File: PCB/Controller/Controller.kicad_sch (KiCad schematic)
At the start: 2 parts

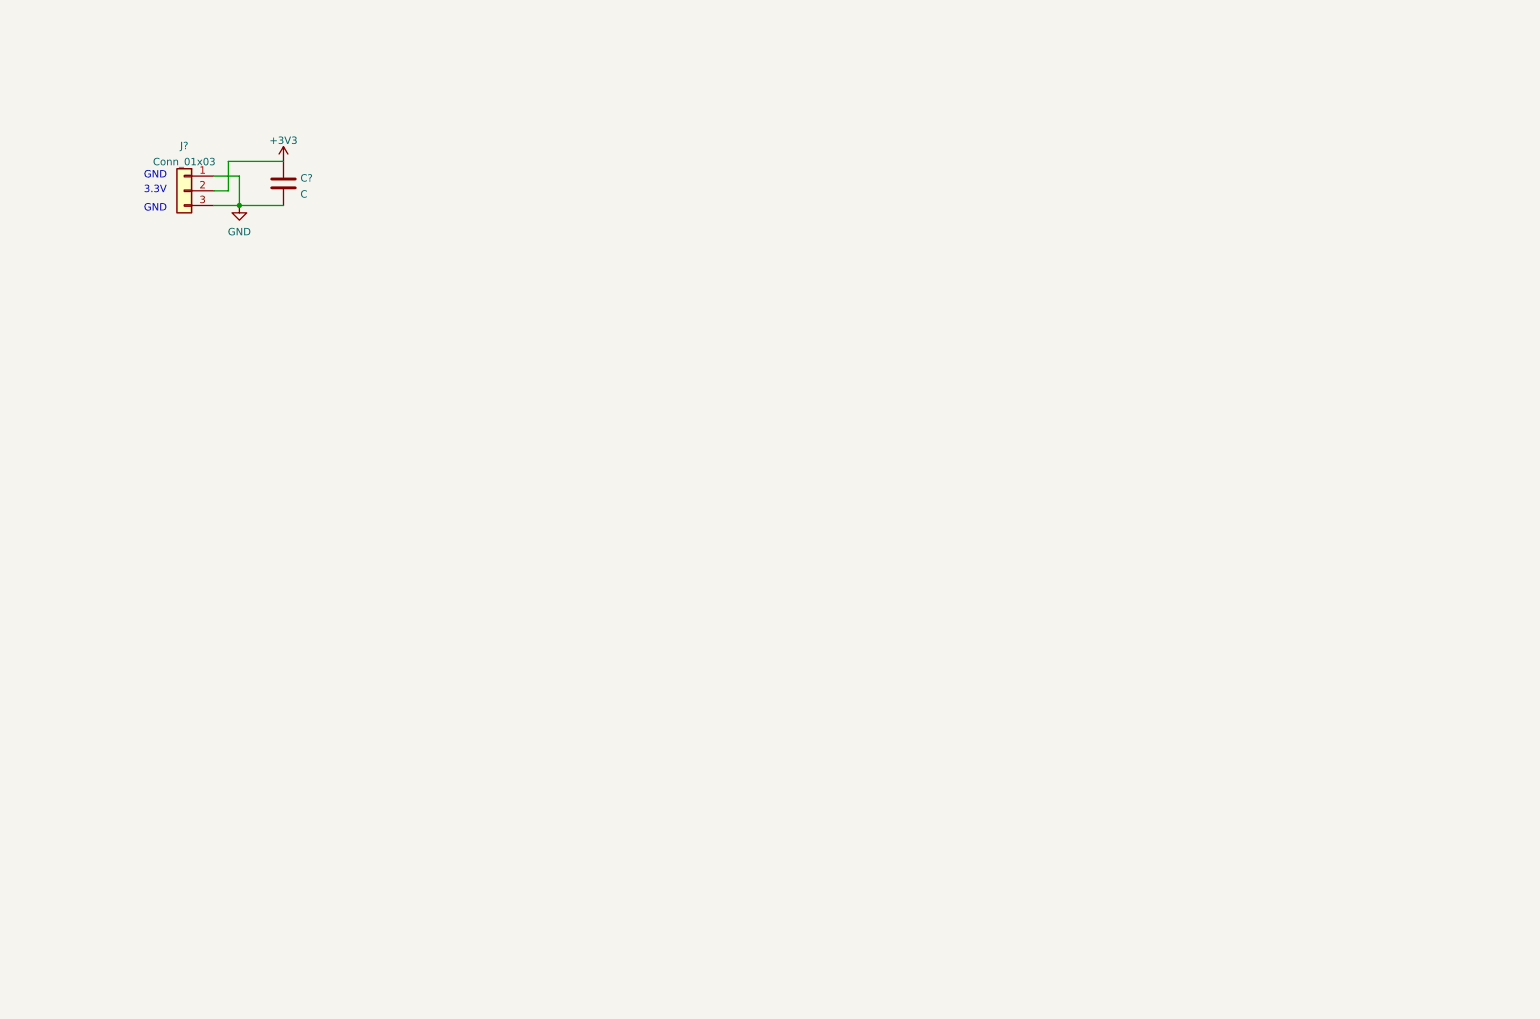
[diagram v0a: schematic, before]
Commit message: sample bdf font script.
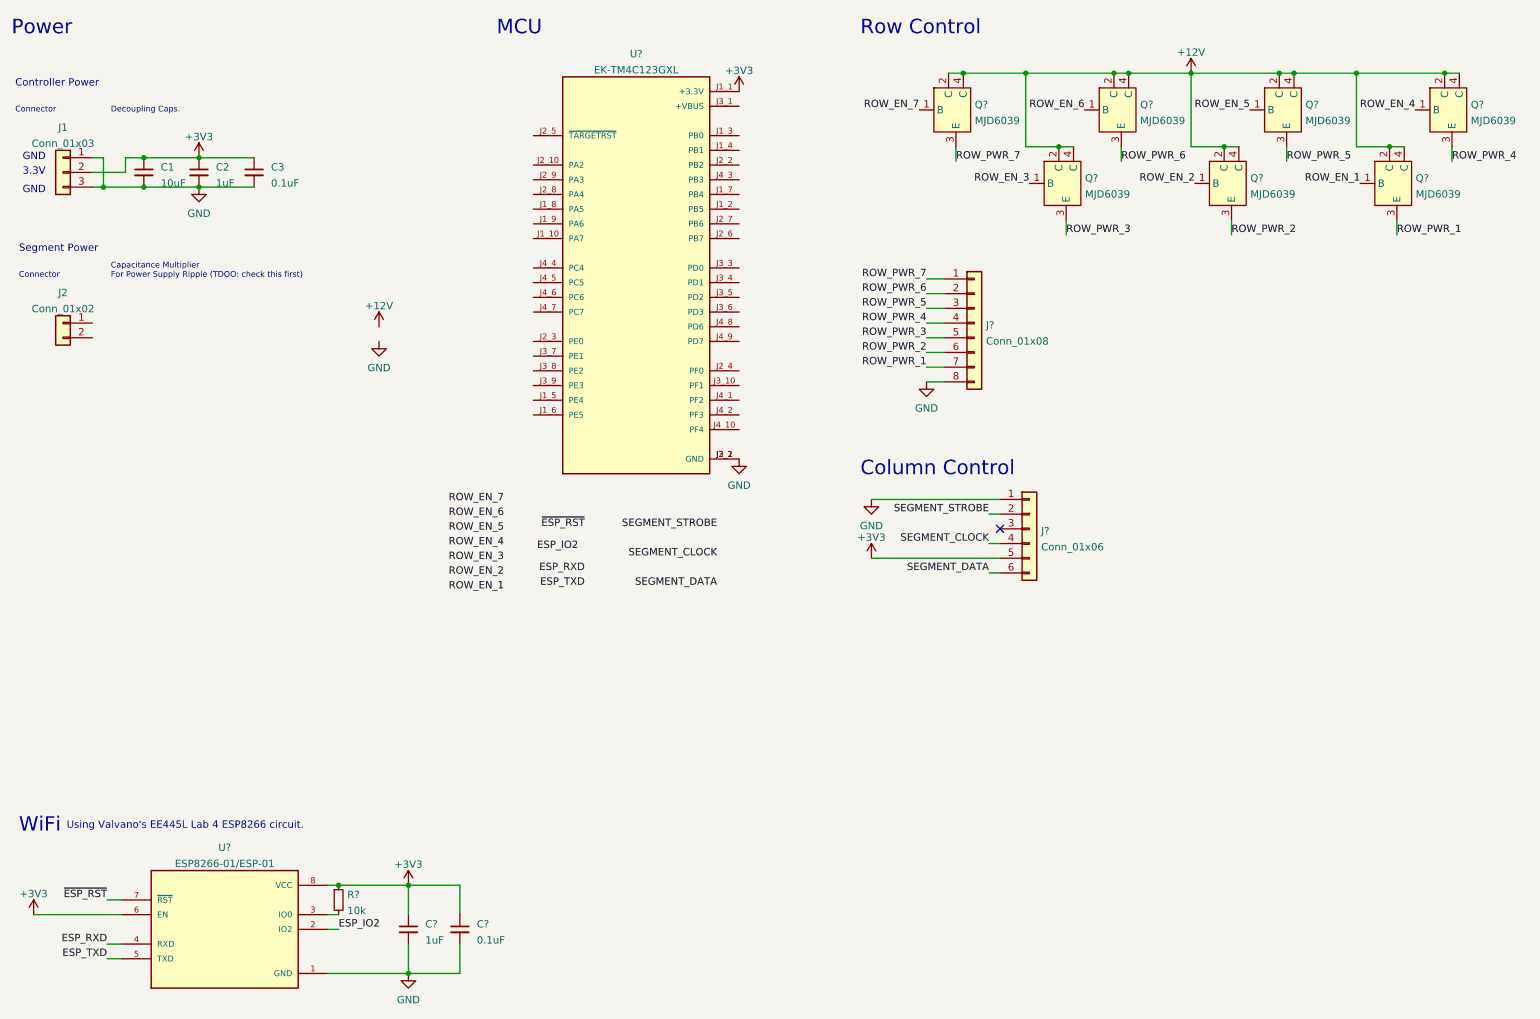
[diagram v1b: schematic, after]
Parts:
- added C1: 10uF, symbol Device:C_Small
- added C3, C?: 0.1uF, symbol Device:C_Small
- added C?: 1uF, symbol Device:C_Small
- added J2: Conn_01x02, symbol Connector_Generic:Conn_01x02
- added J?: Conn_01x06, symbol Connector_Generic:Conn_01x06
- added J?: Conn_01x08, symbol Connector_Generic:Conn_01x08
- added Q? (x7): MJD6039, symbol MJD6039:MJD6039
- added R?: 10k, symbol Device:R_Small
- added U?: ESP8266-01/ESP-01, Footprints:XCVR_ESP8266-01_ESP-01, symbol ESP8266-01_ESP-01:ESP8266-01{brace}slash}ESP-01
- added U?: EK-TM4C123GXL, Footprints:MODULE_EK-TM4C123GXL, symbol EK-TM4C123GXL:EK-TM4C123GXL
- C2: renamed from C?; value C -> 1uF; symbol Device:C -> Device:C_Small
- gave numbers to parts that had none: 1
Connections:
- net +3V3: now also C1.1, C3.1, C?.1, C?.1, J?.5 (Pin_5), R?.1, U?.6 (EN), U?.8 (VCC), U?.J1_1 (+3.3V)
- net GND: now also C1.2, C3.2, C?.2, C?.2, J?.1 (Pin_1), J?.8 (Pin_8), U?.1 (GND), U?.J2_1 (GND), U?.J3_2 (GND)
- new net: R?.2, U?.3 (IO0)
- new net +12V: Q?.2 (C), Q?.2 (C), Q?.2 (C), Q?.2 (C), Q?.2 (C), Q?.2 (C), Q?.2 (C), Q?.4 (C), Q?.4 (C), Q?.4 (C), Q?.4 (C), Q?.4 (C), Q?.4 (C), Q?.4 (C)
- new net ESP_IO2: U?.2 (IO2)
- new net ESP_RXD: U?.4 (RXD)
- new net ESP_TXD: U?.5 (TXD)
- new net ROW_EN_1: Q?.1 (B)
- new net ROW_EN_2: Q?.1 (B)
- new net ROW_EN_3: Q?.1 (B)
- new net ROW_EN_4: Q?.1 (B)
- new net ROW_EN_5: Q?.1 (B)
- new net ROW_EN_6: Q?.1 (B)
- new net ROW_EN_7: Q?.1 (B)
- new net ROW_PWR_1: J?.7 (Pin_7), Q?.3 (E)
- new net ROW_PWR_2: J?.6 (Pin_6), Q?.3 (E)
- new net ROW_PWR_3: J?.5 (Pin_5), Q?.3 (E)
- new net ROW_PWR_4: J?.4 (Pin_4), Q?.3 (E)
- new net ROW_PWR_5: J?.3 (Pin_3), Q?.3 (E)
- new net ROW_PWR_6: J?.2 (Pin_2), Q?.3 (E)
- new net ROW_PWR_7: J?.1 (Pin_1), Q?.3 (E)
- new net SEGMENT_CLOCK: J?.4 (Pin_4)
- new net SEGMENT_DATA: J?.6 (Pin_6)
- new net SEGMENT_STROBE: J?.2 (Pin_2)
- new net ~{ESP_RST}: U?.7 (~{RST})
- no-connect marks 0 -> 1
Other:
- note added: "Capacitance Multiplier For Power Supply Ripple (TDOO: check this first)"
- note added: "Column Control"
- note added: "Connector"
- note added: "Controller Power"
- note added: "Decoupling Caps."
- note added: "MCU"
- note added: "Power"
- note added: "Row Control"
- note added: "Segment Power"
- note added: "Using Valvano's EE445L Lab 4 ESP8266 circuit."
- note added: "WiFi"
- company: (none) -> IEEE RAS UT
- title: (none) -> Marquee Signboard Controller
- moved on the sheet: C2, J1

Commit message: finished v1.0.0 of marquee controller.
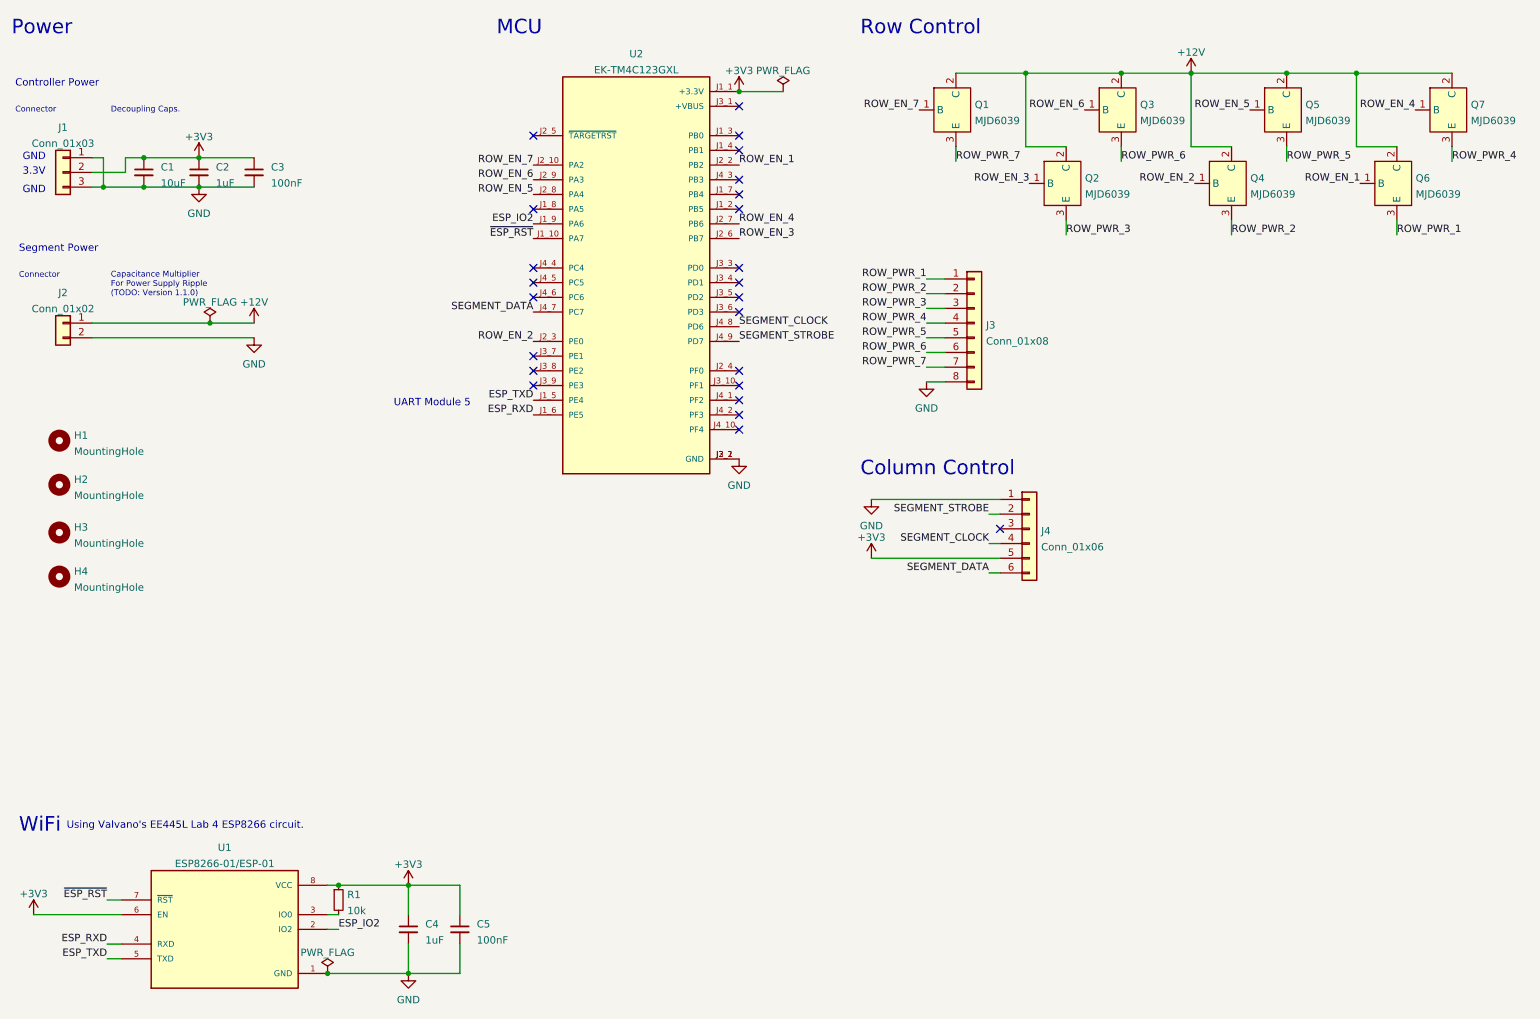
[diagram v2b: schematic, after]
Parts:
- added H1, H2, H3, H4: MountingHole, MountingHole:MountingHole_2.2mm_M2, symbol Mechanical:MountingHole
- C1: footprint (none) -> Capacitor_SMD:C_0805_2012Metric; Distributor (none) -> JLCPCB; JLCPCB BOM (none) -> 1; LCSC Part (none) -> C15850; Manufacturer (none) -> Samsung Electro-Mechanics; Part Number (none) -> CL21A106KAYNNNE; Projected Cost (none) -> 0.0148
- C2: footprint (none) -> Capacitor_SMD:C_0805_2012Metric; Distributor (none) -> JLCPCB; JLCPCB BOM (none) -> 1; LCSC Part (none) -> C28323; Manufacturer (none) -> Samsung Electro-Mechanics; Part Number (none) -> CL21B105KBFNNNE; Projected Cost (none) -> 0.0096
- C3: value 0.1uF -> 100nF; footprint (none) -> Capacitor_SMD:C_0805_2012Metric; Distributor (none) -> JLCPCB; JLCPCB BOM (none) -> 1; LCSC Part (none) -> C49678; Manufacturer (none) -> Yageo; Part Number (none) -> CC0805KRX7R9BB104; Projected Cost (none) -> 0.0048
- C4: renamed from C?; footprint (none) -> Capacitor_SMD:C_0805_2012Metric; Distributor (none) -> JLCPCB; JLCPCB BOM (none) -> 1; LCSC Part (none) -> C28323; Manufacturer (none) -> Samsung Electro-Mechanics; Part Number (none) -> CL21B105KBFNNNE; Projected Cost (none) -> 0.0096
- C5: renamed from C?; value 0.1uF -> 100nF; footprint (none) -> Capacitor_SMD:C_0805_2012Metric; Distributor (none) -> JLCPCB; JLCPCB BOM (none) -> 1; LCSC Part (none) -> C49678; Manufacturer (none) -> Yageo; Part Number (none) -> CC0805KRX7R9BB104; Projected Cost (none) -> 0.0048
- J1: footprint (none) -> Connector_PinHeader_2.54mm:PinHeader_1x03_P2.54mm_Vertical
- J2: footprint (none) -> Connector_Wire:SolderWire-2.5sqmm_1x02_P7.2mm_D2.4mm_OD3.6mm
- J3: renamed from J?; footprint (none) -> Footprints:SolderWire-2sqmm_1x08_P7.8mm_D2mm_OD3.9mm
- J4: renamed from J?; footprint (none) -> Connector_Wire:SolderWire-2.5sqmm_1x06_P8.8mm_D2.4mm_OD4.4mm
- Q1, Q2, Q3, Q4, Q5, Q6, Q7: renamed from Q?; footprint (none) -> Package_TO_SOT_SMD:TO-252-3_TabPin2; Distributor (none) -> Mouser; JLCPCB BOM (none) -> 0; Manufacturer (none) -> ONSEMI; Part Number (none) -> MJD6039T4G; Projected Cost (none) -> 0.9; Purchase Page (none) -> https://www.mouser.com/ProductDetail/onsemi/MJD6039T4G?qs=H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
- R1: renamed from R?; footprint (none) -> Resistor_SMD:R_0805_2012Metric; Distributor (none) -> JLCPCB; JLCPCB BOM (none) -> 1; LCSC Part (none) -> C17724; Manufacturer (none) -> Uniroyal Elec; Part Number (none) -> 0805W8F510KT5E; Projected Cost (none) -> 0.0038
- U1: renamed from U?; Distributor (none) -> Mouser; JLCPCB BOM (none) -> 0; MANUFACTURER AI-Thinker -> (none); MAXIMUM_PACKAGE_HEIGHT 11.2 mm -> (none); Manufacturer (none) -> SparkFun; PARTREV V1.2 -> (none); Part Number (none) -> WRL-17146; Projected Cost (none) -> 6.95; Purchase Page (none) -> https://www.mouser.com/ProductDetail/SparkFun/WRL-17146?qs=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; STANDARD Manufacturer recommendations or IPC 7351B -> (none)
- U2: renamed from U?; Alternative Part (none) -> https://www.ti.com/tool/EK-TM4C123GXL; Distributor (none) -> Mouser; JLCPCB BOM (none) -> 0; MANUFACTURER Texas Instruments -> (none); MAXIMUM_PACKAGE_HIEGHT N/A -> (none); Manufacturer (none) -> Texas Instruments; PARTREV April 2013 -> (none); Part Number (none) -> EK-TM4C123GXL; Projected Cost (none) -> 22.60; Purchase Page (none) -> https://www.mouser.com/ProductDetail/Texas-Instruments/EK-T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; STANDARD Manufacturer Recommendations -> (none)
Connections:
- net +12V: now also J2.1 (Pin_1); no longer Q1.4 (C), Q2.4 (C), Q3.4 (C), Q4.4 (C), Q5.4 (C), Q6.4 (C), Q7.4 (C)
- net ESP_IO2: now also U2.J1_9 (PA6)
- net ESP_RXD: now also U2.J1_6 (PE5)
- net ESP_TXD: now also U2.J1_5 (PE4)
- net GND: now also J2.2 (Pin_2)
- net ROW_EN_1: now also U2.J2_2 (PB2)
- net ROW_EN_2: now also U2.J2_3 (PE0)
- net ROW_EN_3: now also U2.J2_6 (PB7)
- net ROW_EN_4: now also U2.J2_7 (PB6)
- net ROW_EN_5: now also U2.J2_8 (PA4)
- net ROW_EN_6: now also U2.J2_9 (PA3)
- net ROW_EN_7: now also U2.J2_10 (PA2)
- net ROW_PWR_1: now also J3.1 (Pin_1); no longer J3.7 (Pin_7)
- net ROW_PWR_2: now also J3.2 (Pin_2); no longer J3.6 (Pin_6)
- net ROW_PWR_3: now also J3.3 (Pin_3); no longer J3.5 (Pin_5)
- net ROW_PWR_5: now also J3.5 (Pin_5); no longer J3.3 (Pin_3)
- net ROW_PWR_6: now also J3.6 (Pin_6); no longer J3.2 (Pin_2)
- net ROW_PWR_7: now also J3.7 (Pin_7); no longer J3.1 (Pin_1)
- net SEGMENT_CLOCK: now also U2.J4_8 (PD6)
- net SEGMENT_DATA: now also U2.J4_7 (PC7)
- net SEGMENT_STROBE: now also U2.J4_9 (PD7)
- net ~{ESP_RST}: now also U2.J1_10 (PA7)
- no-connect marks 1 -> 24
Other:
- note added: "Capacitance Multiplier For Power Supply Ripple (TODO: Version 1.1.0)"
- note added: "UART Module 5"
- note removed: "Capacitance Multiplier For Power Supply Ripple (TDOO: check this first)"
